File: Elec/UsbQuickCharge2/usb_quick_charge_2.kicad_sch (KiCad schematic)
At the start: 15 parts, among them J1 USB_B_Micro, J2 Conn_01x03, Q1 NX7002AKA, SW1 SW_SPDT

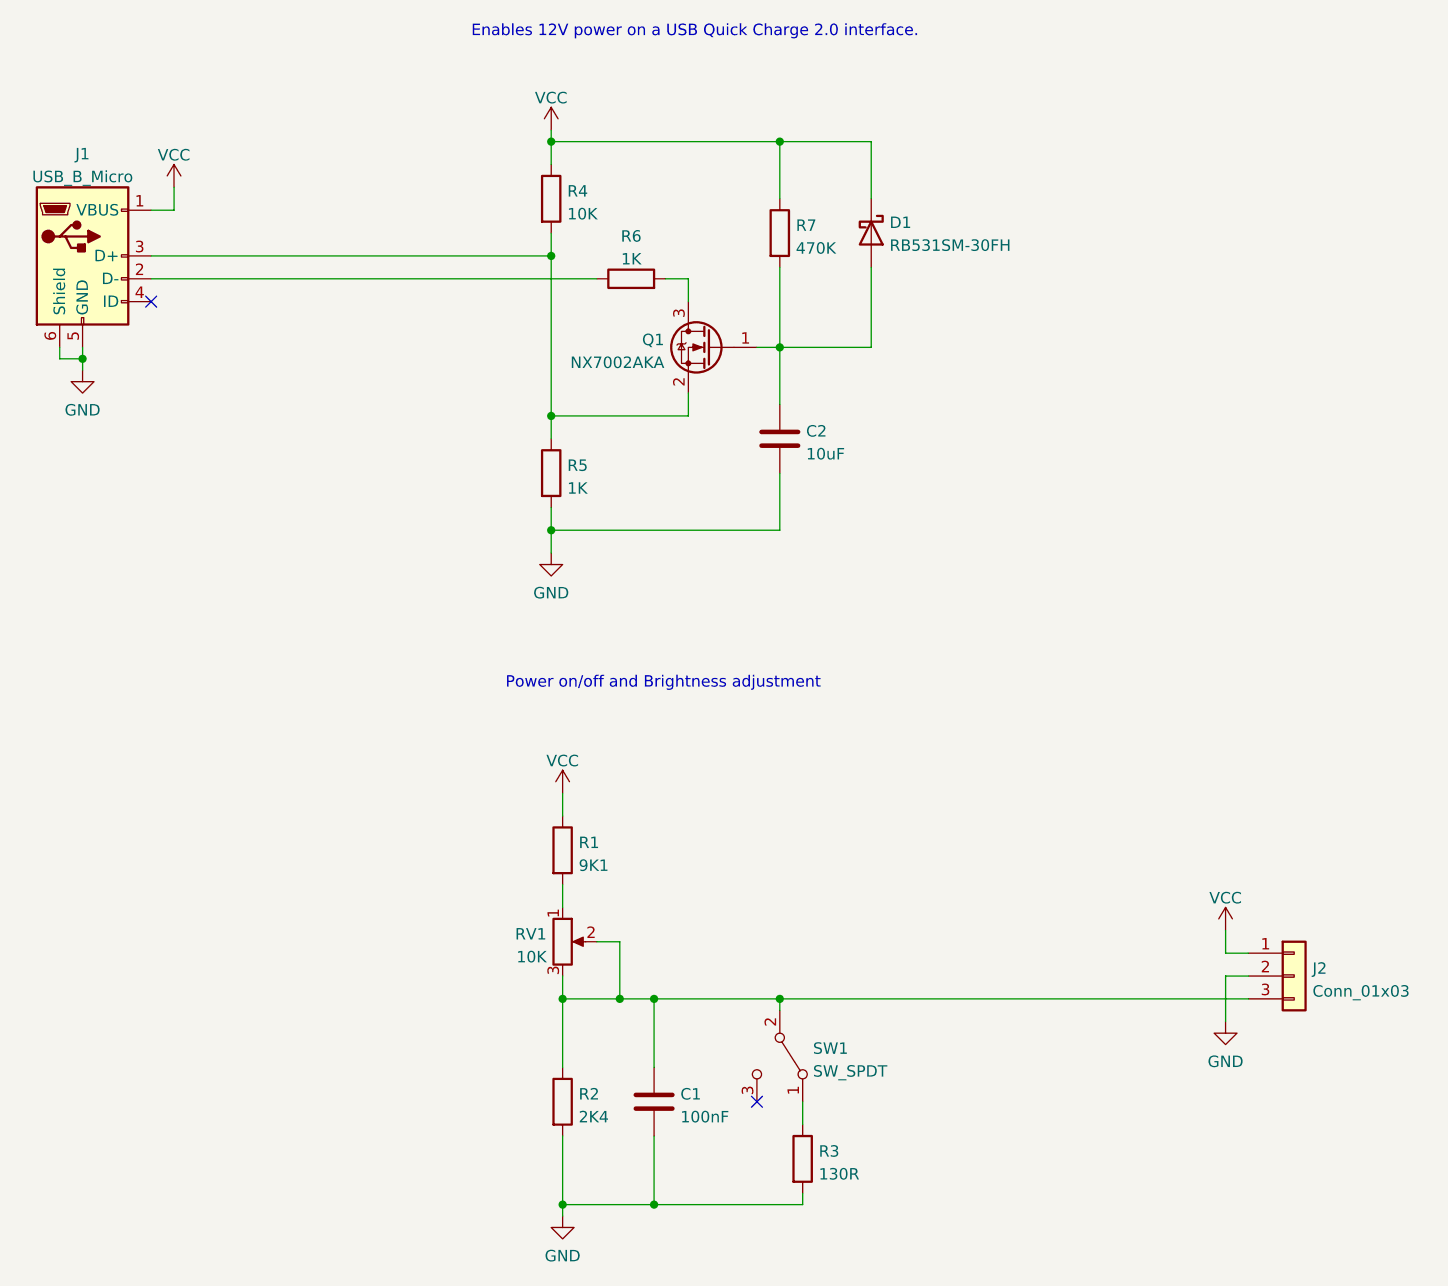
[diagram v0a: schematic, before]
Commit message: delete packages3d folders
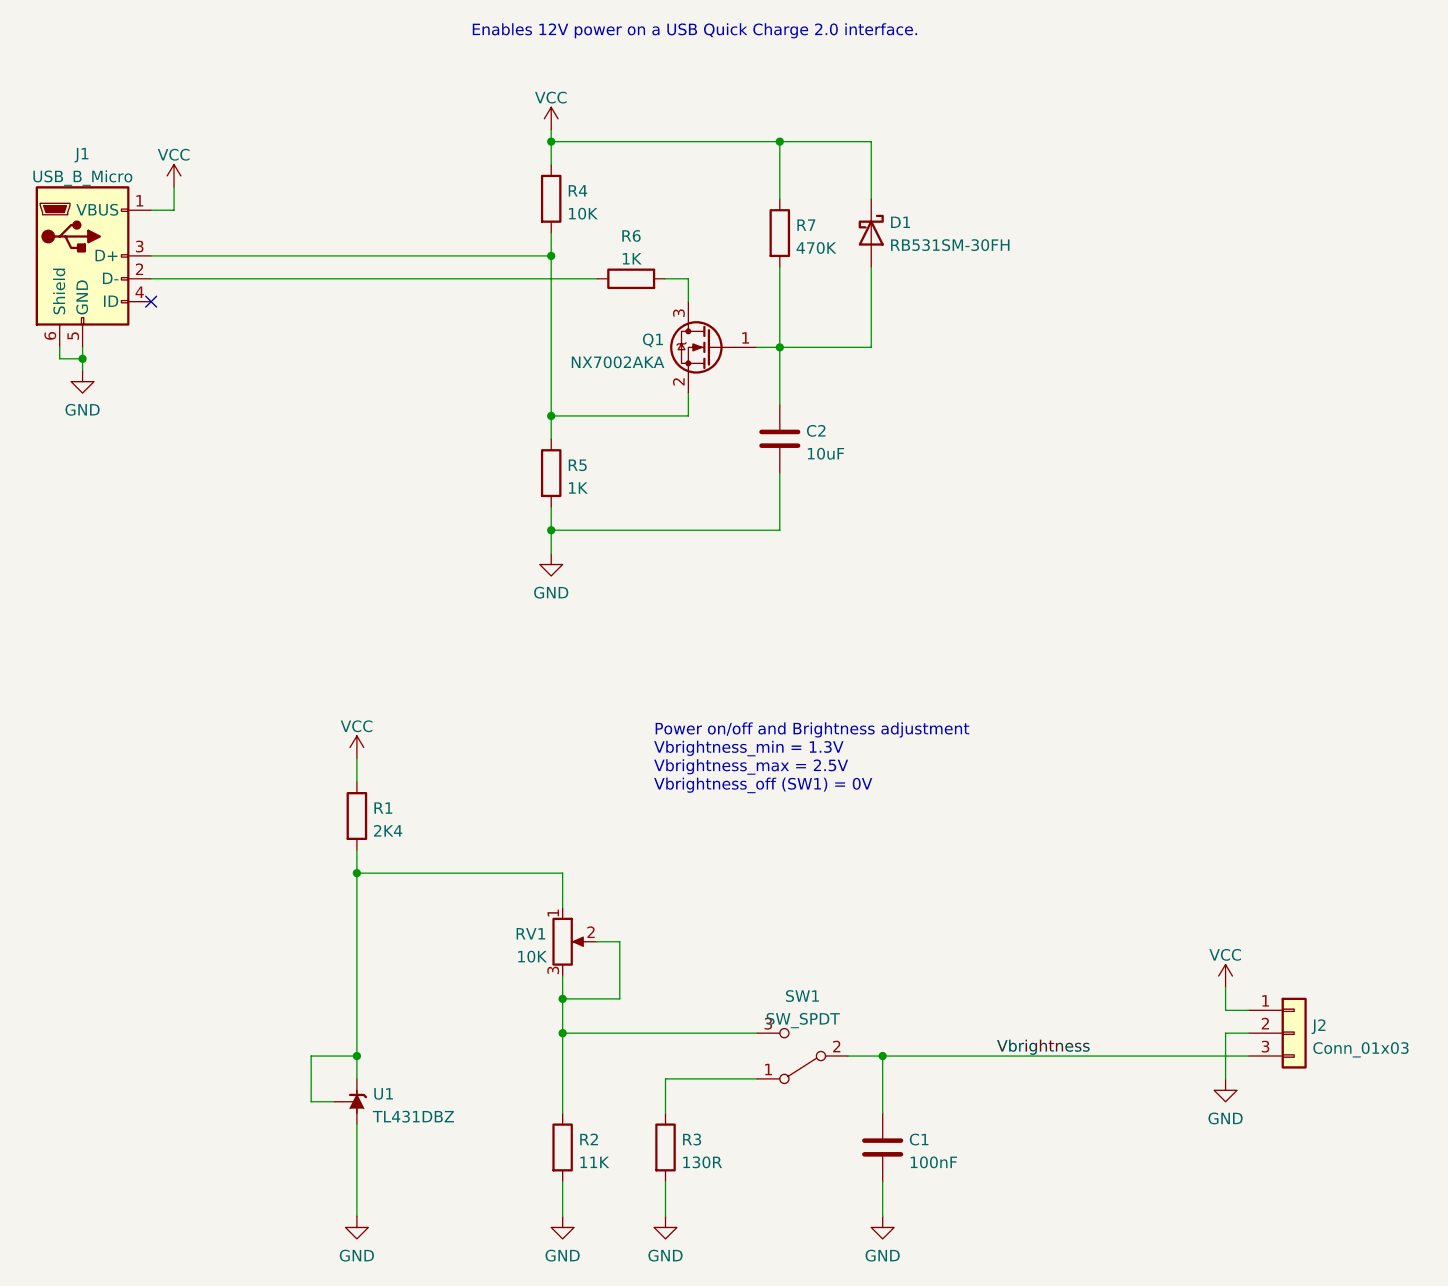
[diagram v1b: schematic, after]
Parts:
- added U1: TL431DBZ, Package_TO_SOT_SMD:SOT-23, symbol Reference_Voltage:TL431DBZ
- C1: footprint Capacitor_SMD:C_01005_0402Metric_Pad0.57x0.30mm_HandSolder -> Capacitor_SMD:C_0402_1005Metric_Pad0.74x0.62mm_HandSolder
- R1: value 9K1 -> 2K4
- R2: value 2K4 -> 11K
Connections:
- net GND: now also U1.3 (A)
- net at R1.2, RV1.1: now also U1.1 (K), U1.2 (REF)
- net at R2.1, RV1.2, RV1.3: now also SW1.3 (C); no longer C1.1, J2.3 (Pin_3), SW1.2 (B)
- new net Vbrightness: C1.1, J2.3 (Pin_3), SW1.2 (B)
- no-connect marks 2 -> 1
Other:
- note added: "Power on/off and Brightness adjustment Vbrightness_min = 1.3V Vbrightness_max = 2.5V Vbrightness_off (SW1) = 0V"
- note removed: "Power on/off and Brightness adjustment"
- moved on the sheet: C1, J2, R2, R3, SW1
